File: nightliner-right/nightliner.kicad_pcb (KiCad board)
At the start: 2 copper layers, 154.8 x 116.1 mm, 87 parts, among them J1 TYPE-C-31-M-12, J2 Battery, J3 Serial, P1 ISP_Prog, SW1 pinky_top, SW10 inner_home, SW11 pinky_bottom, SW12 ring_bottom, SW13 middle_bottom, SW14 index_bottom, SW15 inner_bottom, SW16 outer_top, SW17 outer_home, SW18 near_thumb, SW19 home_thumb, SW2 ring_top, SW20 far_thumb, SW21 ON_OFF, SW22 RESET, SW3 middle_top, SW4 index_top, SW5 inner_top, SW6 pinky_home, SW7 ring_home, SW8 middle_home, SW9 index_home, U1 holyiot-18010, U2 TVS2200DRV, U3 USBLC6-2SC6, U4 BQ24075RGT, U5 XC6220B331MR

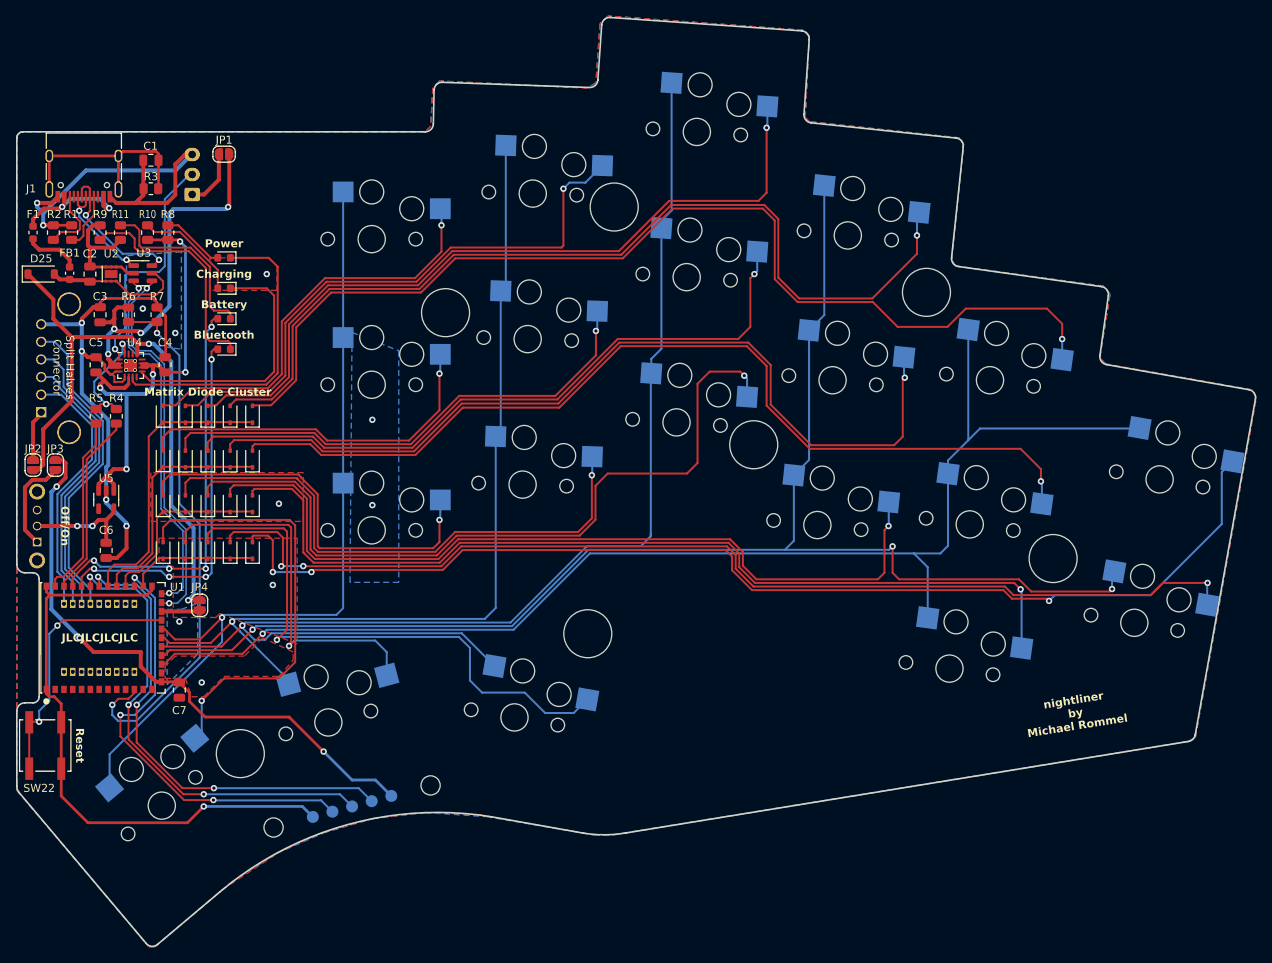
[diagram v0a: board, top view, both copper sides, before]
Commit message: fix: rework right case, fix outline
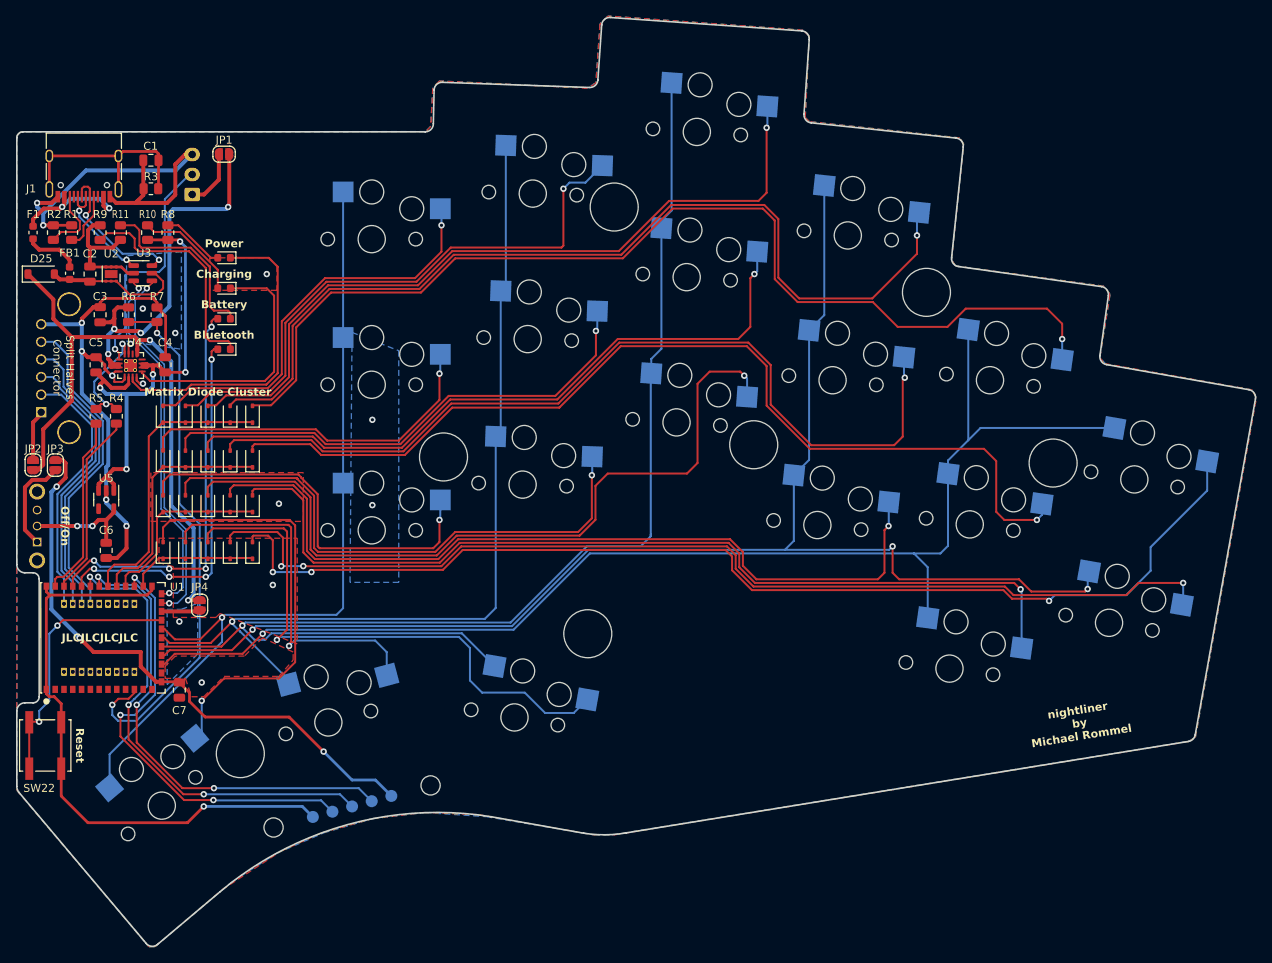
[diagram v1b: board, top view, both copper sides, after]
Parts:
- moved H5 18.0 mm to (88.9, 78.7)
- moved H1 11.9 mm to (165.1, 79.5)
- moved SW16 3.16 mm to (175.3, 81.5)
- moved SW17 3.16 mm to (172.1, 99.5)
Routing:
- net Net-(D6-A): track 119.0 -> 122.7 mm
- net COL0: track 164.5 -> 161.3 mm
- net Net-(D16-A): track 143.2 -> 140.1 mm
- net COL1: track 178.8 -> 175.7 mm
- net Net-(D17-A): track 135.2 -> 132.2 mm
- net GND: track 210.8 -> 213.7 mm, vias 16 -> 19
- net D-: track 47.6 -> 46.3 mm
- net D+: track 45.9 -> 44.9 mm
- net Net-(D10-A): track 45.7 -> 45.0 mm
- net Net-(D22-K): track 39.1 -> 39.7 mm

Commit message: fix: final version, create production gerbers
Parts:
- D1, D10, D11, D12, D13, D14, D15, D16, D17, D18, D19, D2, D20, D3, D4, D5, D6, D7, D8, D9: value D_Small -> 1N4148WS
- H1: footprint miro_keyboard:StandOff_6mm_M3 -> nightliner:StandOff_6mm_M3
- H2, H3, H4, H5, H6: value MountingHole_M3 -> Standoff_6mm_M3; footprint miro_keyboard:StandOff_6mm_M3 -> nightliner:StandOff_6mm_M3
- H7: value MountingHole_M3 -> Standoff_6mm_M3; footprint miro_keyboard:StandOff_6mm_M3 -> nightliner:StandOff_6mm_M3; moved to B.Cu
- J3: footprint miro_keyboard:MagConn_6pin_right -> nightliner:MagConn_6pin_right
- P1: footprint miro_keyboard:ISP_Programming_Pads -> nightliner:ISP_Programming_Pads
- SW1, SW10, SW11, SW12, SW13, SW14, SW15, SW16, SW17, SW18, SW19, SW2, SW20, SW3, SW4, SW5, SW6, SW7, SW8, SW9: footprint miro_keyboard:Kailh_Choc_CPG135001D02_Hotswap -> nightliner:Kailh_Choc_CPG135001D02_Hotswap
- SW21: footprint miro_keyboard:SW_ROCPU_SK-12D07-5_SPDT_Angled -> nightliner:SW_ROCPU_SK-12D07-5_SPDT_Angled
- SW22: footprint miro_keyboard:SW_Push_1P1T_NO_CK_KSC4xxJ -> nightliner:SW_Push_1P1T_NO_CK_KSC4xxJ
- U1: footprint miro_keyboard:HOLYIOT-18010-UndersidePins-SMD -> nightliner:HOLYIOT-18010-UndersidePins-SMD
- U4: footprint miro_keyboard:VQFN-16-1EP_3x3mm_P0.5mm_EP1.6x1.6mm_ThermalVias -> nightliner:VQFN-16-1EP_3x3mm_P0.5mm_EP1.6x1.6mm_ThermalVias
- moved FB1 0.11 mm to (42.2, 55.9)
- turned H7 to 180 degrees
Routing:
- net Net-(D4-A): track 72.6 -> 79.0 mm
- net COL1: track 175.7 -> 171.3 mm
- net Net-(D18-A): track 71.4 -> 69.4 mm
- net Net-(D17-A): track 132.2 -> 133.7 mm
- net COL2: track 159.1 -> 160.3 mm
- net Net-(D11-A): track 116.1 -> 115.0 mm, vias 1 -> 3
- net Net-(D16-A): track 140.1 -> 139.5 mm
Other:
- board text added: "TEMP"
